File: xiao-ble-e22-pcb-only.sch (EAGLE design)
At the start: 6 parts, among them U1 XIAO-NRF52840/SENSEXIAO-NRF52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, U2 E22-900M30S

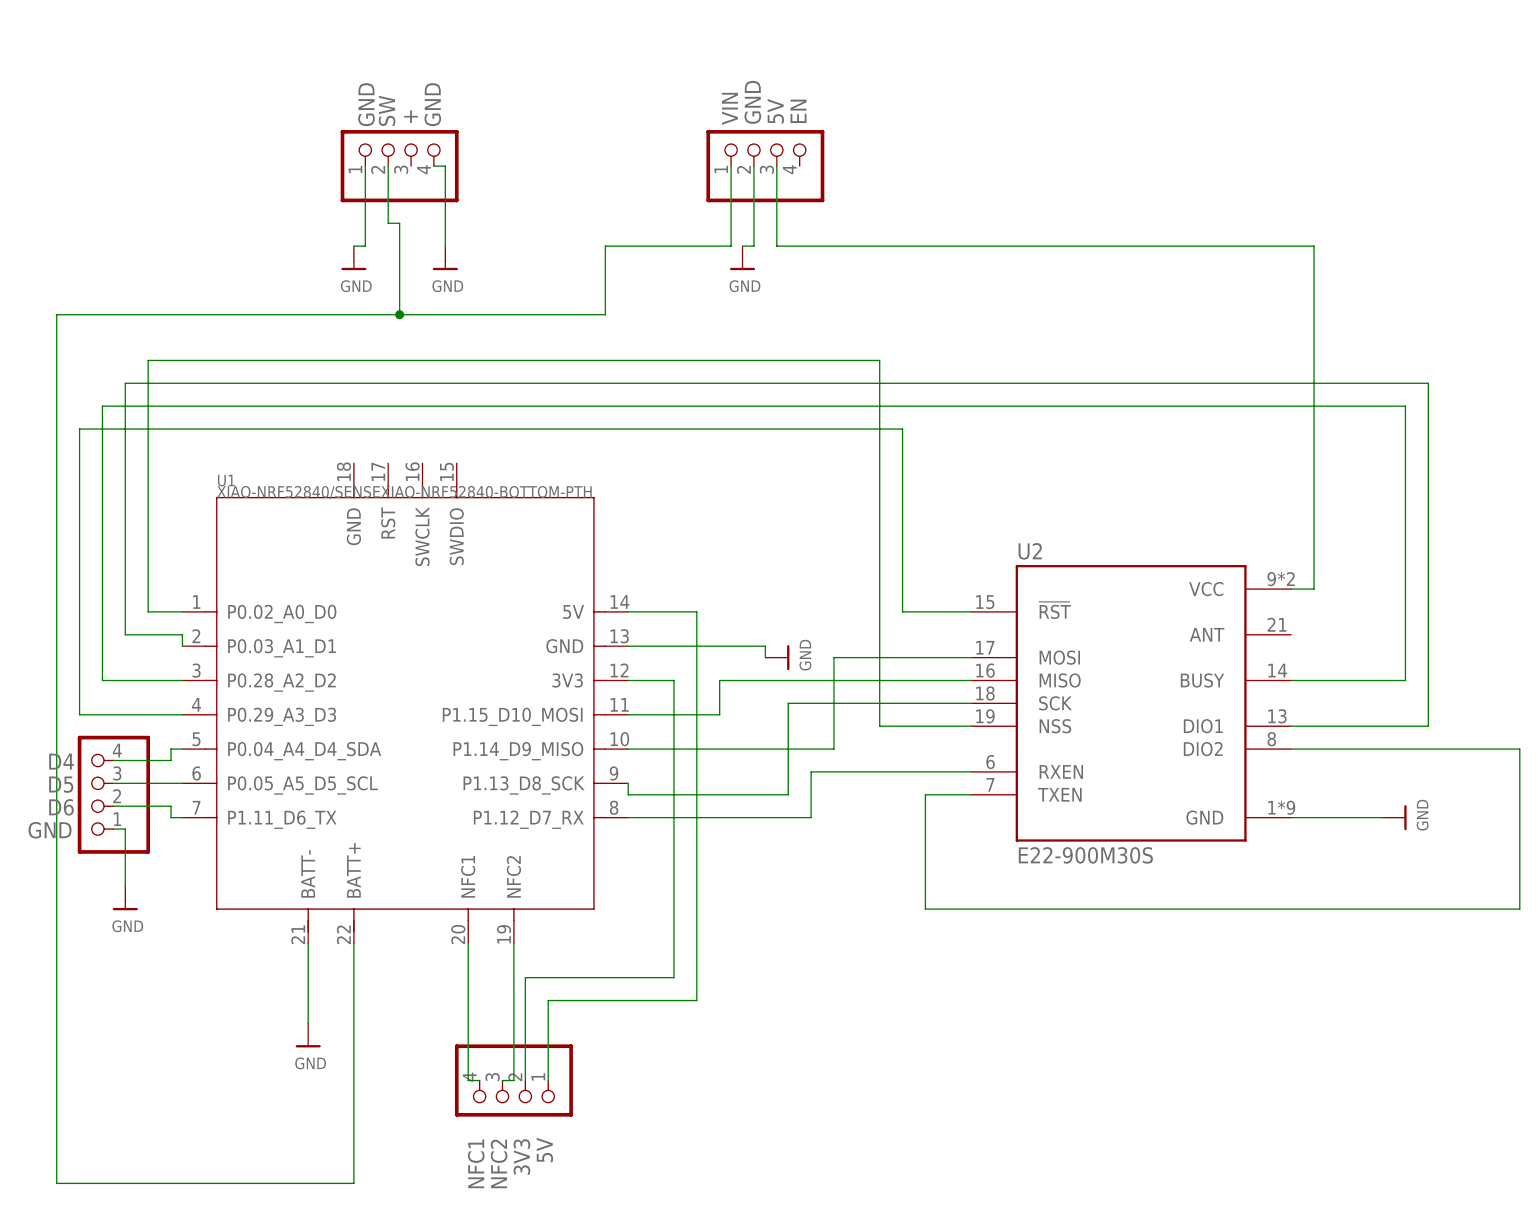
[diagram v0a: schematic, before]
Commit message: Fix issues with board (spacing between XIAO and MiniBoost, MISO/MOSI swapperoo), break out debug pins, reroute
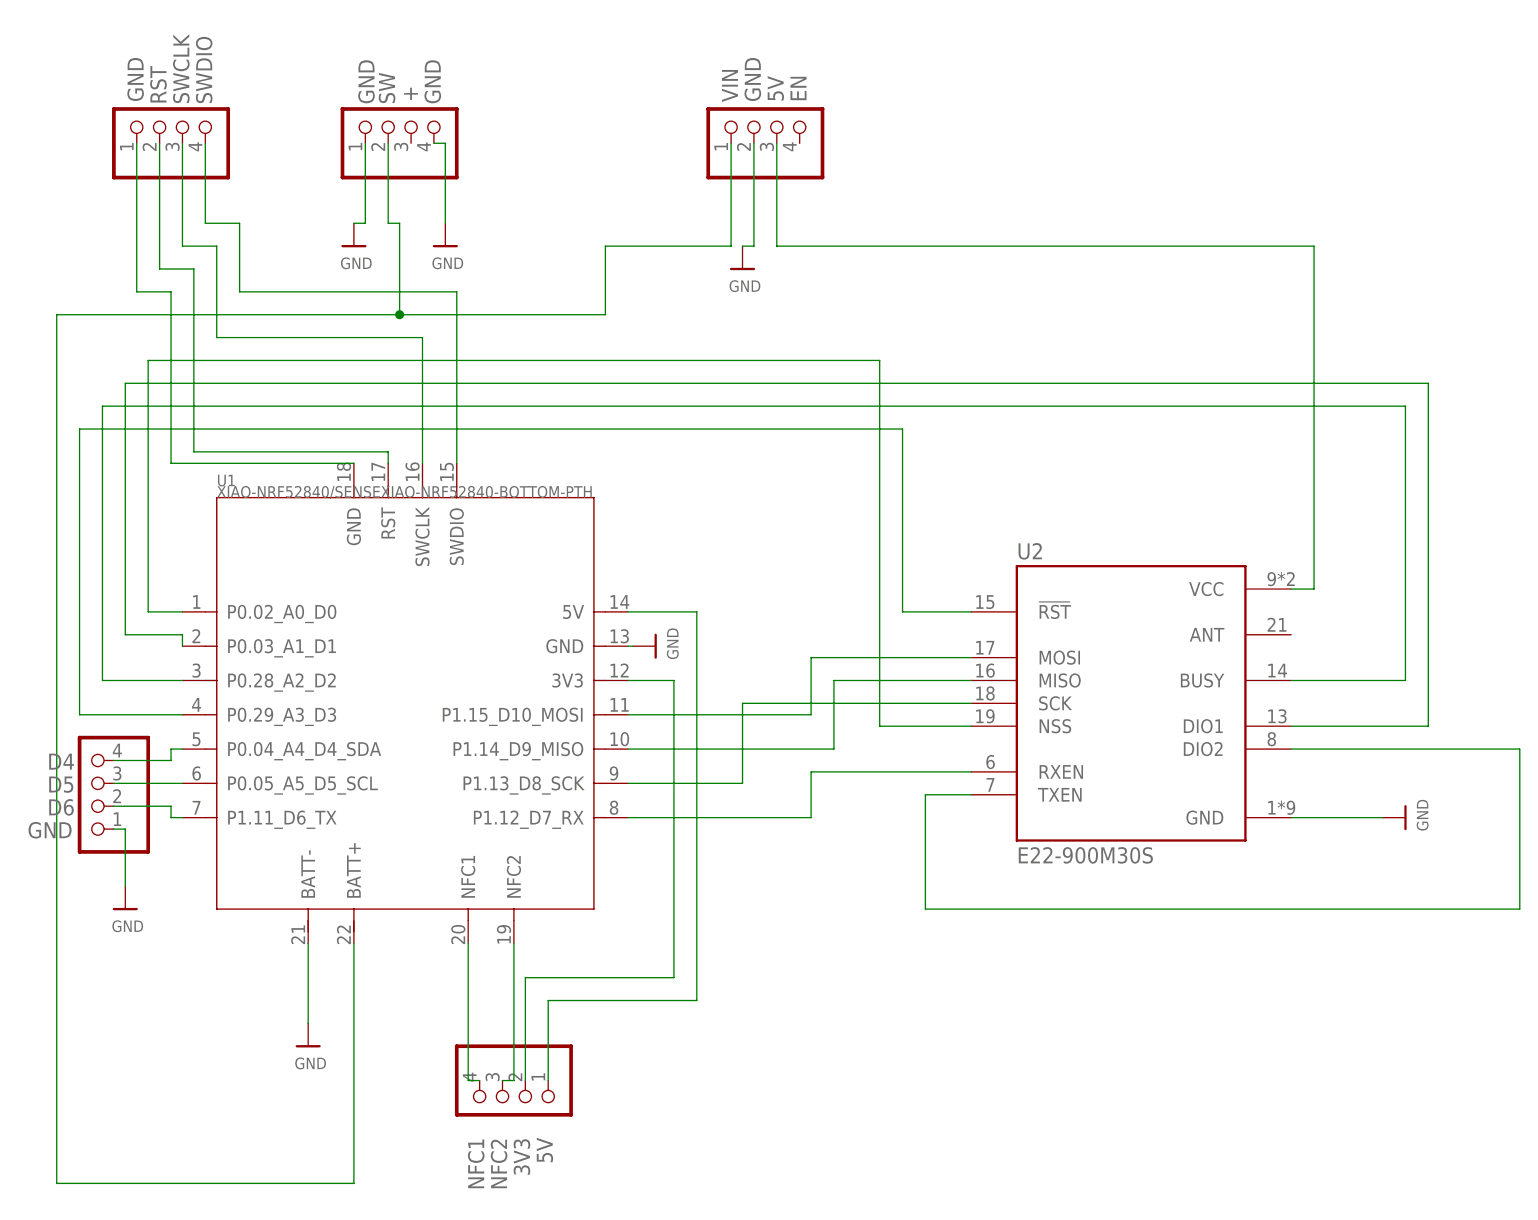
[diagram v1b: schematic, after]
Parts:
- added JP5: GPIO Breakout 2, breakouts:PADS-4
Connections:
- new net N$14: JP5.1, U1.GND@1
- new net N$17: JP5.2, U1.RST
- new net N$21: JP5.3, U1.SWCLK
- new net N$22: JP5.4, U1.SWDIO
- net N$8: now also U1.P1.14_D9_MISO; no longer U1.P1.15_D10_MOSI
- net N$9: now also U1.P1.15_D10_MOSI; no longer U1.P1.14_D9_MISO
